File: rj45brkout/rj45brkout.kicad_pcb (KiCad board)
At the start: 4 copper layers, 27.7 x 20.3 mm, 19 parts, among them J101 RJ45_LEDS, P101 CONN_01X01, P102 CONN_01X01, P103 CONN_01X01, P104 CONN_01X01, P105 CONN_01X01, P106 CONN_01X01, P107 CONN_01X01, P108 CONN_01X01, P109 CONN_01X01, P110 CONN_01X01, P111 CONN_01X01, P112 CONN_01X01

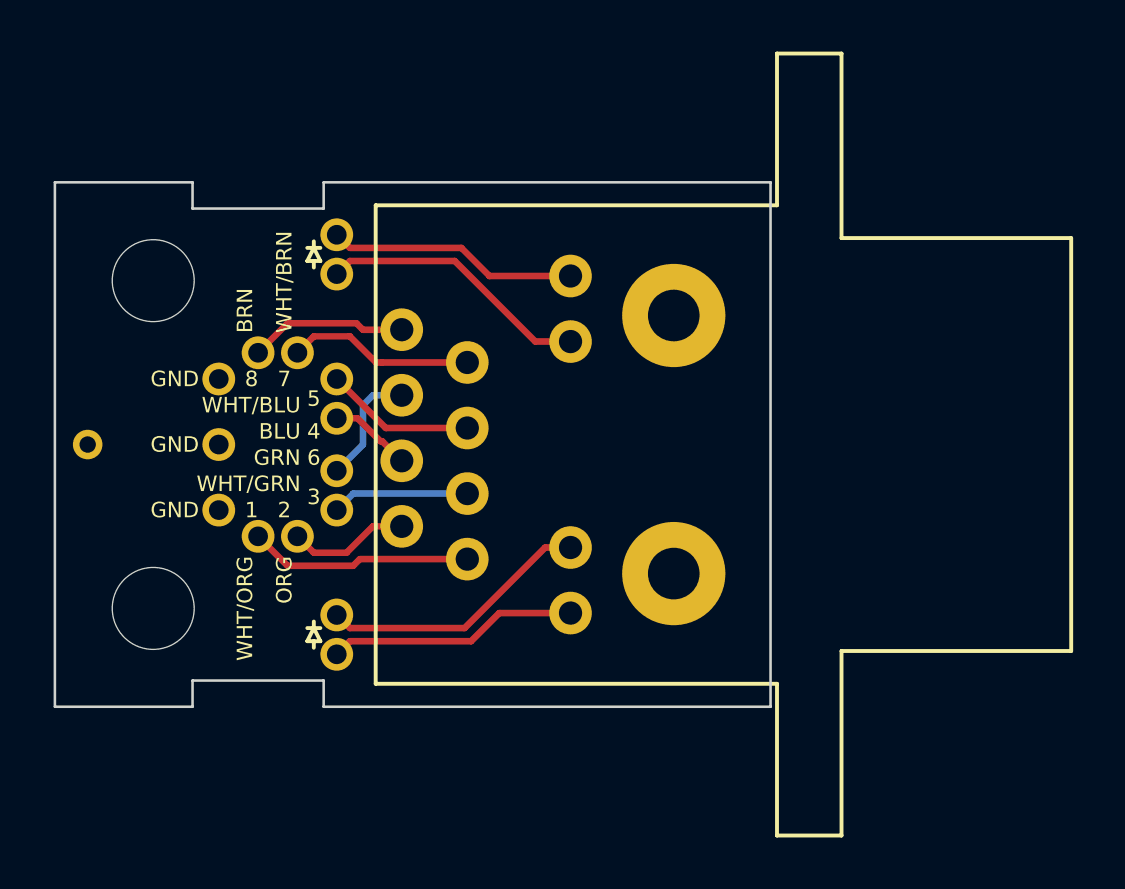
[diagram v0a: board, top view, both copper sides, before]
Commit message: Adjust clearances of ground and vcc pours.
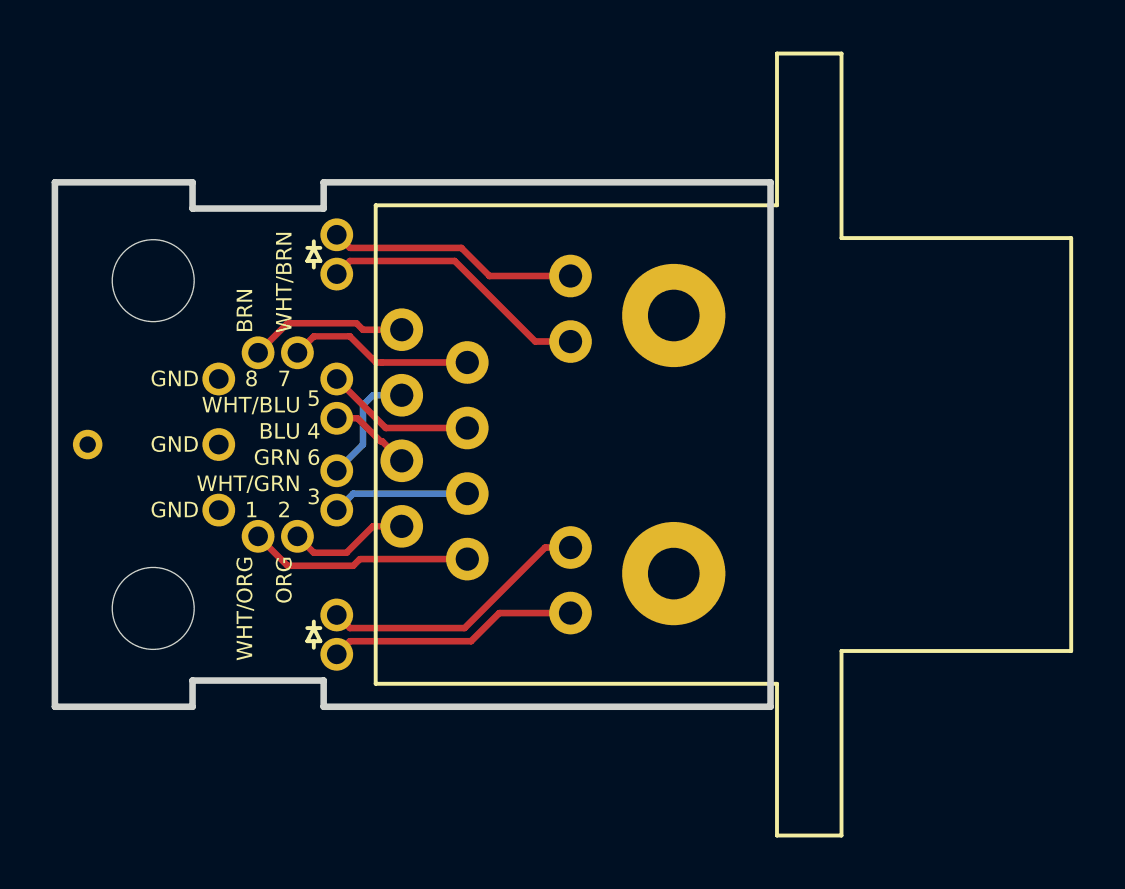
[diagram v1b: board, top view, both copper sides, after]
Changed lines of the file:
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@@
     )
     (fp_circle (center 0 0) (end 3.81 0) (layer Cmts.User) (width 0.381))
-    (pad "" np_thru_hole circle (at 0 0) (size 3.175 3.175) (drill 3.175) (layers *.Cu *.Mask))
+    (pad "" np_thru_hole circle (at 0 0) (size 3.175 3.175) (drill 3.175) (layers *.Cu *.Mask)
+      (clearance 0.508))
   )
   (module local:MountingHole_125mil locked (layer F.Cu)
@@
     )
     (fp_circle (center 0 0) (end 3.81 0) (layer Cmts.User) (width 0.381))
-    (pad "" np_thru_hole circle (at 0 0) (size 3.175 3.175) (drill 3.175) (layers *.Cu *.Mask))
+    (pad "" np_thru_hole circle (at 0 0) (size 3.175 3.175) (drill 3.175) (layers *.Cu *.Mask)
+      (clearance 0.508))
   )
   (module local:rj45-8-pm (layer F.Cu)
@@
     (effects (font (size 0.6 0.6) (thickness 0.127)) (justify right))
   )
-  (gr_line (start 133.604 111.76) (end 128.27 111.76) (layer Edge.Cuts) (width 0.1))
-  (gr_line (start 133.604 91.44) (end 128.27 91.44) (layer Edge.Cuts) (width 0.1))
-  (gr_line (start 138.684 110.744) (end 138.684 111.76) (layer Edge.Cuts) (width 0.1))
-  (gr_line (start 133.604 110.744) (end 138.684 110.744) (layer Edge.Cuts) (width 0.1))
-  (gr_line (start 133.604 111.76) (end 133.604 110.744) (layer Edge.Cuts) (width 0.1))
-  (gr_line (start 138.684 92.456) (end 138.684 91.44) (layer Edge.Cuts) (width 0.1))
-  (gr_line (start 133.604 92.456) (end 138.684 92.456) (layer Edge.Cuts) (width 0.1))
-  (gr_line (start 133.604 91.44) (end 133.604 92.456) (layer Edge.Cuts) (width 0.1))
+  (gr_line (start 133.604 111.76) (end 128.27 111.76) (layer Edge.Cuts) (width 0.254))
+  (gr_line (start 133.604 91.44) (end 128.27 91.44) (layer Edge.Cuts) (width 0.254))
+  (gr_line (start 138.684 110.744) (end 138.684 111.76) (layer Edge.Cuts) (width 0.254))
+  (gr_line (start 133.604 110.744) (end 138.684 110.744) (layer Edge.Cuts) (width 0.254))
+  (gr_line (start 133.604 111.76) (end 133.604 110.744) (layer Edge.Cuts) (width 0.254))
+  (gr_line (start 138.684 92.456) (end 138.684 91.44) (layer Edge.Cuts) (width 0.254))
+  (gr_line (start 133.604 92.456) (end 138.684 92.456) (layer Edge.Cuts) (width 0.254))
+  (gr_line (start 133.604 91.44) (end 133.604 92.456) (layer Edge.Cuts) (width 0.254))
   (gr_text ORG (at 137.16 105.918 90) (layer B.SilkS)
     (effects (font (size 0.6 0.6) (thickness 0.127)) (justify left mirror))
@@
   (gr_line (start 138.303 108.712) (end 138.049 109.22) (layer F.SilkS) (width 0.15))
   (gr_line (start 138.049 108.712) (end 138.557 108.712) (layer F.SilkS) (width 0.15))
-  (gr_line (start 156 91.44) (end 156 111.76) (layer Edge.Cuts) (width 0.1))
-  (gr_line (start 138.684 91.44) (end 156 91.44) (layer Edge.Cuts) (width 0.1))
-  (gr_line (start 128.27 111.76) (end 128.27 91.44) (layer Edge.Cuts) (width 0.1))
-  (gr_line (start 156 111.76) (end 138.684 111.76) (layer Edge.Cuts) (width 0.1))
+  (gr_line (start 156 91.44) (end 156 111.76) (layer Edge.Cuts) (width 0.254))
+  (gr_line (start 138.684 91.44) (end 156 91.44) (layer Edge.Cuts) (width 0.254))
+  (gr_line (start 128.27 111.76) (end 128.27 91.44) (layer Edge.Cuts) (width 0.254))
+  (gr_line (start 156 111.76) (end 138.684 111.76) (layer Edge.Cuts) (width 0.254))
   (segment (start 136.144 105.156) (end 137.287 106.299) (width 0.254) (layer F.Cu) (net 1))
   (segment (start 137.287 106.299) (end 139.827 106.299) (width 0.254) (layer F.Cu) (net 1))
